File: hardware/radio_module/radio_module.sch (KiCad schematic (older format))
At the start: 2 parts, among them U8 conn2x18pcie

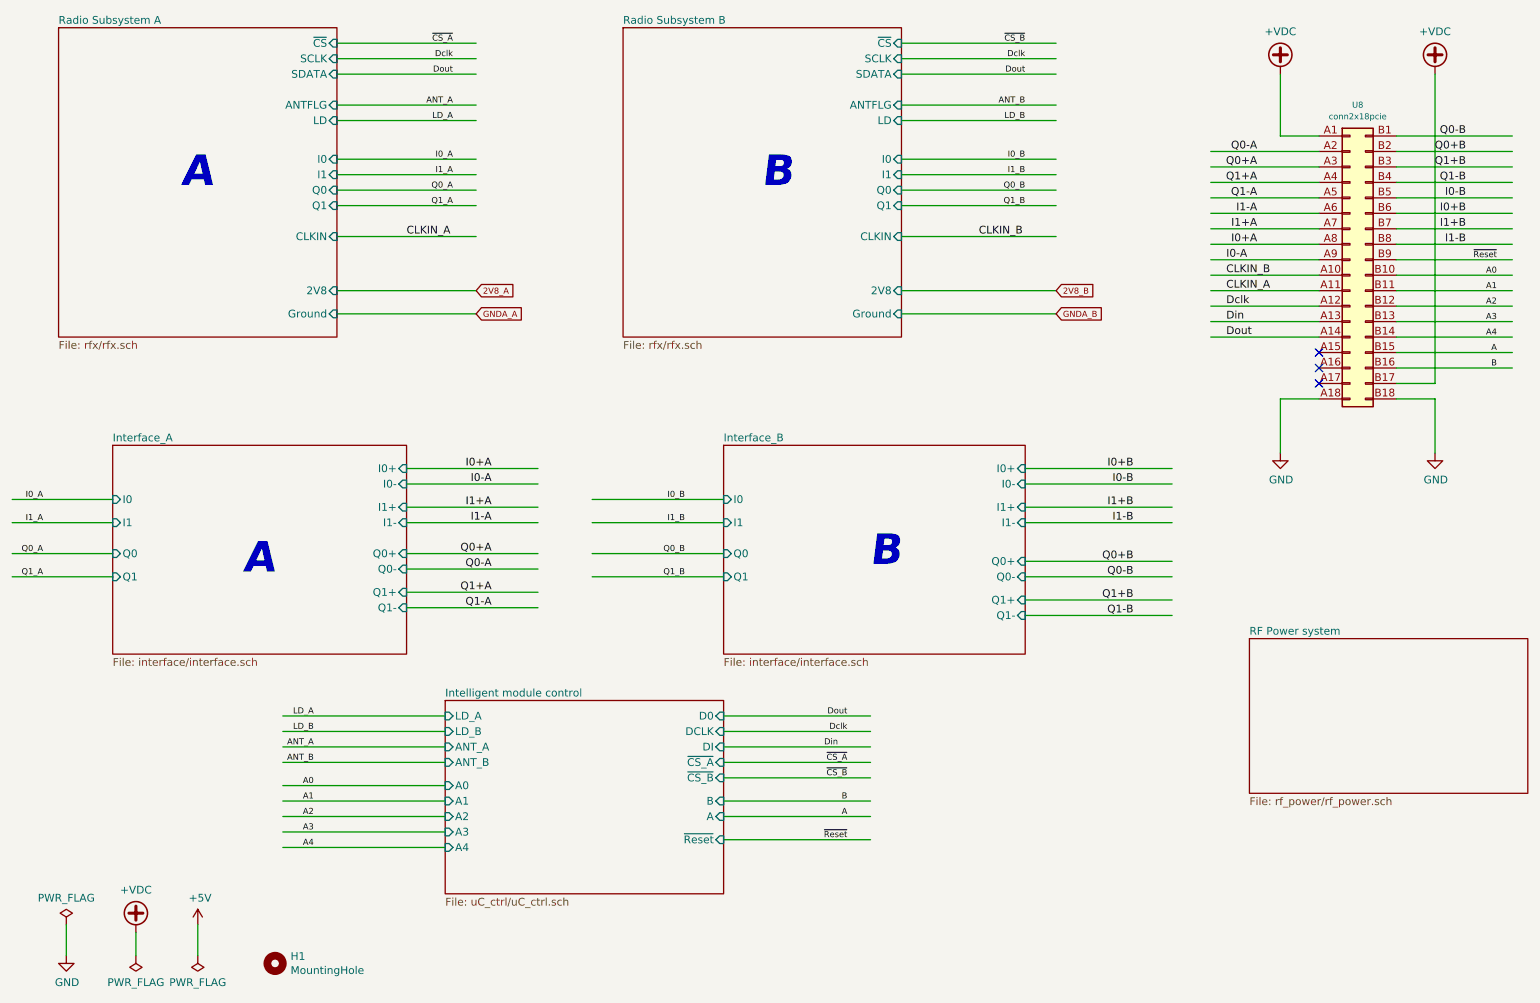
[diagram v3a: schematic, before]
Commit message: Update radio module add extclk, new atmega package, new crystal
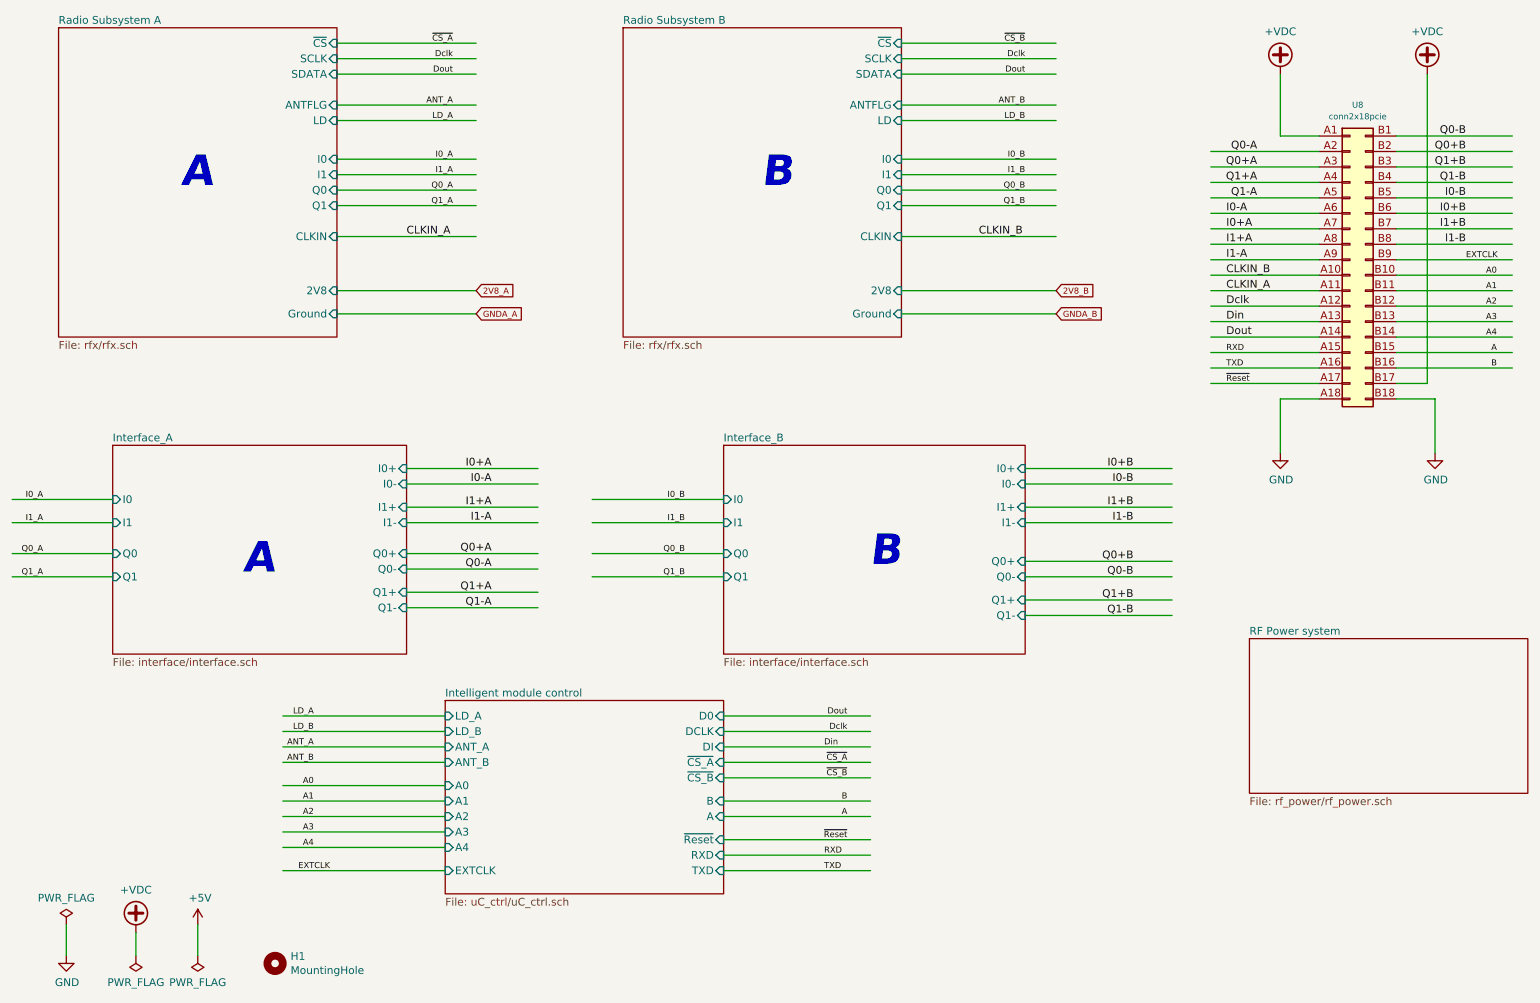
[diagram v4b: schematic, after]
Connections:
- net labels added: EXTCLK, RXD, TXD
- wire segments 105 -> 111
- no-connect marks 3 -> 0
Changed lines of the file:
@@
 F17 "~Reset" I R 5450 6450 50
 F18 "DI" I R 5450 5850 50
+F19 "RXD" I R 5450 6550 50
+F20 "TXD" I R 5450 6650 50
+F21 "EXTCLK" I L 3650 6650 50
 $EndSheet
 $Sheet
@@
 L power:+VDC #PWR03
 U 1 1 5DBFB032
-P 10050 1500
-F 0 "#PWR03" H 10050 1400 50  0001 C CNN
-F 1 "+VDC" H 10050 1775 50  0000 C CNN
-F 2 "" H 10050 1500 50  0001 C CNN
-F 3 "" H 10050 1500 50  0001 C CNN
-	1    10050 1500
+P 10000 1500
+F 0 "#PWR03" H 10000 1400 50  0001 C CNN
+F 1 "+VDC" H 10000 1775 50  0000 C CNN
+F 2 "" H 10000 1500 50  0001 C CNN
+F 3 "" H 10000 1500 50  0001 C CNN
+	1    10000 1500
 	1    0    0    -1
 $EndComp
@@
 	2050 7200 2050 7000
 Wire Wire Line
-	10050 3500 9800 3500
-Wire Wire Line
-	10050 1500 10050 3500
+	10000 3500 9800 3500
+Wire Wire Line
+	10000 1500 10000 3500
 Wire Wire Line
 	9800 3000 10550 3000
@@
 Wire Wire Line
 	9800 2800 10550 2800
-Wire Wire Line
-	9800 2700 10550 2700
 Text Label 10450 3000 2    39   ~ 0
 A2
@@
 Text Label 10450 2800 2    39   ~ 0
 A0
-Text Label 10450 2700 2    39   ~ 0
-~Reset
-NoConn ~ 9300 3300
-NoConn ~ 9300 3400
-NoConn ~ 9300 3500
 Wire Wire Line
 	2950 2900 3850 2900
@@
 Wire Wire Line
 	9300 2200 8600 2200
-Wire Wire Line
-	9300 2300 8600 2300
-Wire Wire Line
-	9300 2400 8600 2400
-Wire Wire Line
-	9300 2500 8600 2500
-Wire Wire Line
-	9300 2600 8600 2600
 Text Label 8900 2000 2    50   ~ 0
 Q0-A
@@
 Text Label 8900 2300 2    50   ~ 0
 Q1-A
-Text Label 8900 2400 2    50   ~ 0
-I1-A
-Text Label 8900 2500 2    50   ~ 0
-I1+A
-Text Label 8900 2600 2    50   ~ 0
-I0+A
 Wire Wire Line
 	9800 1900 10550 1900
@@
 $EndComp
 Wire Wire Line
-	9300 2700 8600 2700
-Text Label 8700 2700 0    50   ~ 0
-I0-A
-Wire Wire Line
 	9300 2900 8600 2900
 Text Label 8700 2900 0    50   ~ 0
@@
 Text Label 8700 3000 0    50   ~ 0
 Dclk
+Wire Wire Line
+	9300 2300 8600 2300
+Wire Wire Line
+	9300 2400 8600 2400
+Wire Wire Line
+	9300 2500 8600 2500
+Wire Wire Line
+	9300 2600 8600 2600
+Wire Wire Line
+	9300 2700 8600 2700
+Text Label 8700 2400 0    50   ~ 0
+I0-A
+Text Label 8700 2500 0    50   ~ 0
+I0+A
+Text Label 8700 2600 0    50   ~ 0
+I1+A
+Text Label 8700 2700 0    50   ~ 0
+I1-A
+Wire Wire Line
+	5450 6550 6400 6550
+Wire Wire Line
+	5450 6650 6400 6650
+Text Label 6100 6550 0    39   ~ 0
+RXD
+Text Label 6100 6650 0    39   ~ 0
+TXD
+Wire Wire Line
+	9300 3300 8600 3300
+Wire Wire Line
+	9300 3400 8600 3400
+Text Label 8700 3300 0    39   ~ 0
+RXD
+Text Label 8700 3400 0    39   ~ 0
+TXD
+Wire Wire Line
+	9300 3500 8600 3500
+Text Label 8700 3500 0    39   ~ 0
+~Reset
+Wire Wire Line
+	3650 6650 2600 6650
+Text Label 2700 6650 0    39   ~ 0
+EXTCLK
+Wire Wire Line
+	9800 2700 10550 2700
+Text Label 10250 2700 0    39   ~ 0
+EXTCLK
 $EndSCHEMATC
